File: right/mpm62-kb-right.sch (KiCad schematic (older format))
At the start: 72 parts, among them J1 Conn_01x04_Male, SW1 SW_Push, U1 MCP23018-E_SP

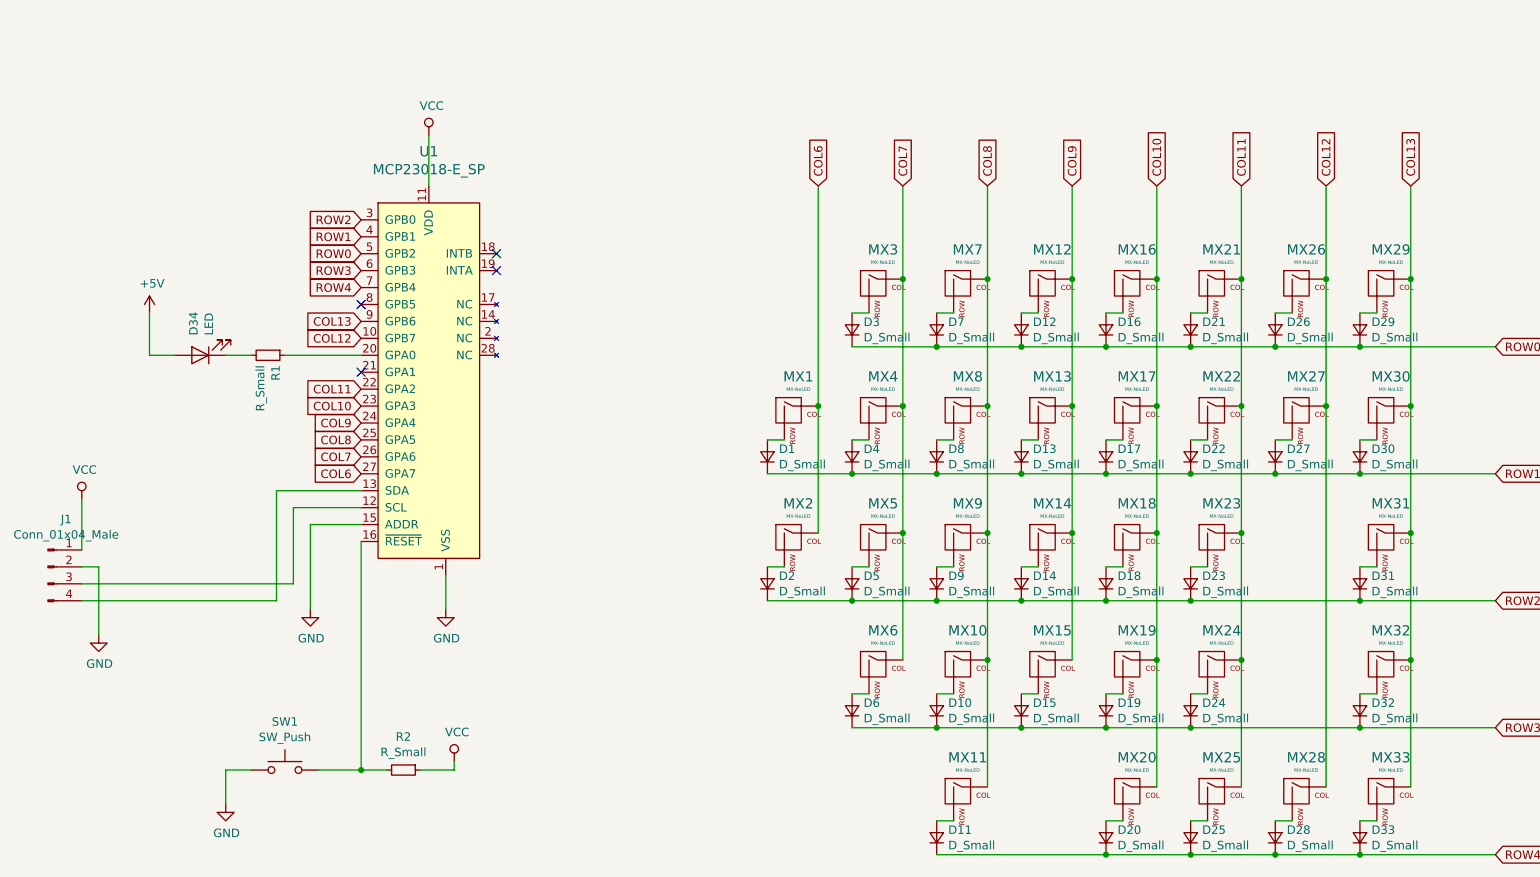
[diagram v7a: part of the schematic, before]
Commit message: Fix issues on right side: 1. Remove reset switch and connect reset directly to vcc - switch was not useful and added complexity. 2. Inverted spacebar stabilizer holes (previous commit did not mention that this was done also on the left side). 3. LED was connected to wrong power bus. 4. Resistor size was smaller than typical TH resistors. 5. Add header pins for ground and vcc for debugging. 6. Some minor routing cleanups.
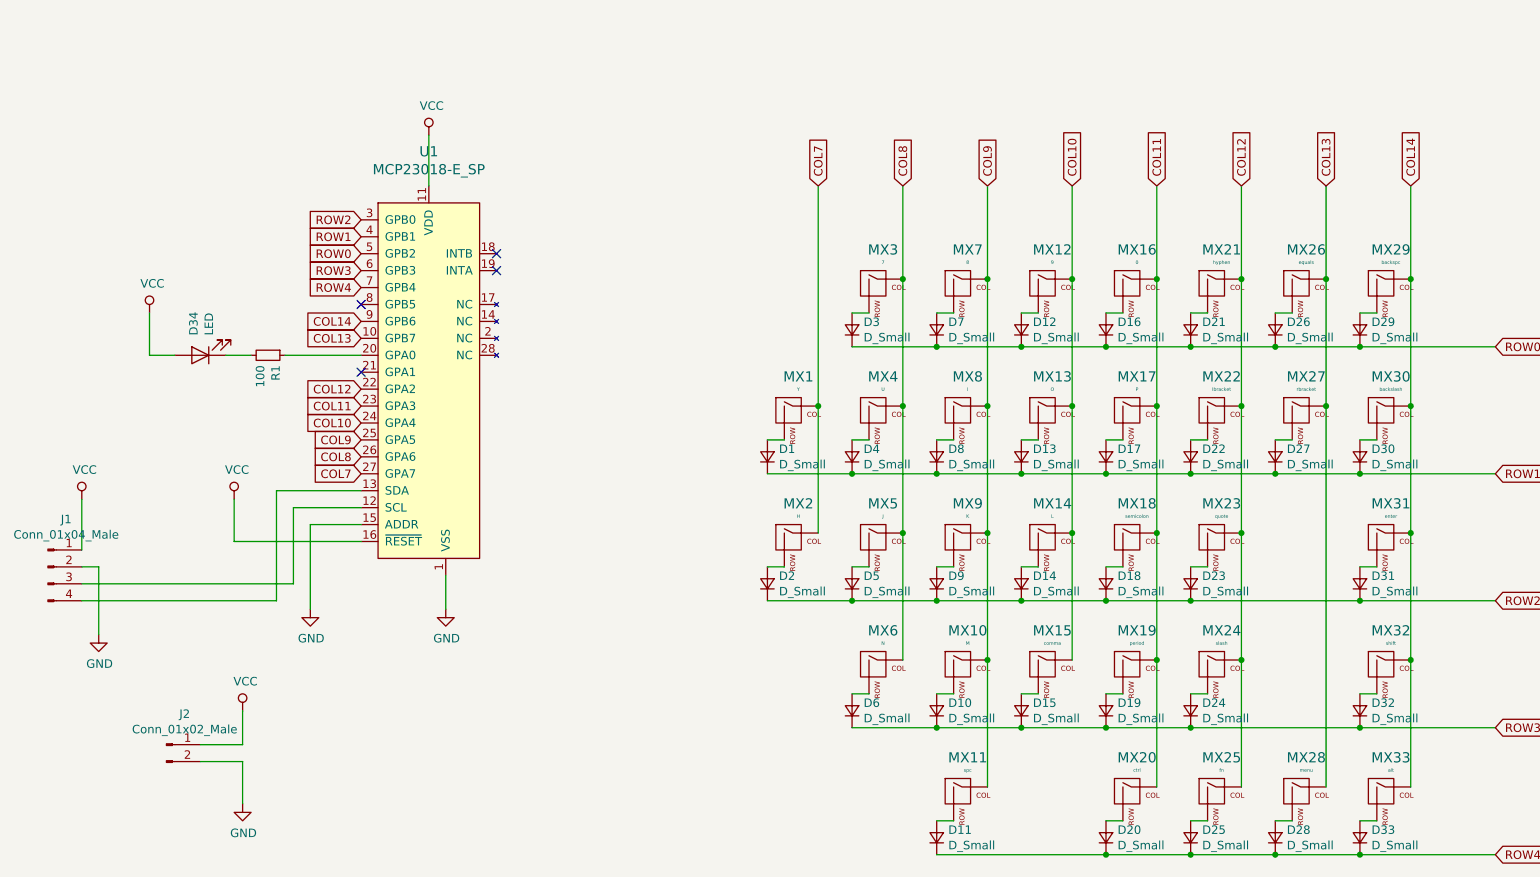
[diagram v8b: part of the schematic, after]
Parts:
- removed R2: R_Small, Resistor_THT:R_Axial_DIN0204_L3.6mm_D1.6mm_P5.08mm_Horizontal, symbol Device:R_Small
- removed SW1: SW_Push, random-keyboard-parts:SKQG-1155865, symbol Switch:SW_Push
- added J2: Conn_01x02_Male, Connector_PinHeader_2.54mm:PinHeader_1x02_P2.54mm_Vertical, symbol Connector:Conn_01x02_Male
- MX1: value MX-NoLED -> Y
- MX10: value MX-NoLED -> M
- MX11: value MX-NoLED -> spc; footprint MX_Alps_Hybrid:MX-3U-NoLED -> MX_Alps_Hybrid:MX-3U-ReversedStabilizers-NoLED
- MX12: value MX-NoLED -> 9
- MX13: value MX-NoLED -> O
- MX14: value MX-NoLED -> L
- MX15: value MX-NoLED -> comma
- MX16: value MX-NoLED -> 0
- MX17: value MX-NoLED -> P
- MX18: value MX-NoLED -> semicolon
- MX19: value MX-NoLED -> period
- MX2: value MX-NoLED -> H
- MX20: value MX-NoLED -> ctrl
- MX21: value MX-NoLED -> hyphen
- MX22: value MX-NoLED -> lbracket
- MX23: value MX-NoLED -> quote
- MX24: value MX-NoLED -> slash
- MX25: value MX-NoLED -> fn
- MX26: value MX-NoLED -> equals
- MX27: value MX-NoLED -> rbracket
- MX28: value MX-NoLED -> menu
- MX29: value MX-NoLED -> backspc
- MX3: value MX-NoLED -> 7
- MX30: value MX-NoLED -> backslash
- MX31: value MX-NoLED -> enter
- MX32: value MX-NoLED -> shift
- MX33: value MX-NoLED -> alt
- MX4: value MX-NoLED -> U
- MX5: value MX-NoLED -> J
- MX6: value MX-NoLED -> N
- MX7: value MX-NoLED -> 8
- MX8: value MX-NoLED -> I
- MX9: value MX-NoLED -> K
- R1: value R_Small -> 100; footprint Resistor_THT:R_Axial_DIN0204_L3.6mm_D1.6mm_P5.08mm_Horizontal -> Resistor_THT:R_Axial_DIN0207_L6.3mm_D2.5mm_P7.62mm_Horizontal
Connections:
- net +5V is gone; now on net VCC: D34.2 (A)
- net COL6 is gone; now on net COL7: MX1.1 (COL), MX2.1 (COL), U1.27 (GPA7)
- net COL10: now also MX12.1 (COL), MX13.1 (COL), MX14.1 (COL), MX15.1 (COL), U1.24 (GPA4); no longer MX16.1 (COL), MX17.1 (COL), MX18.1 (COL), MX19.1 (COL), MX20.1 (COL), U1.23 (GPA3)
- net COL11: now also MX16.1 (COL), MX17.1 (COL), MX18.1 (COL), MX19.1 (COL), MX20.1 (COL), U1.23 (GPA3); no longer MX21.1 (COL), MX22.1 (COL), MX23.1 (COL), MX24.1 (COL), MX25.1 (COL), U1.22 (GPA2)
- net COL12: now also MX21.1 (COL), MX22.1 (COL), MX23.1 (COL), MX24.1 (COL), MX25.1 (COL), U1.22 (GPA2); no longer MX26.1 (COL), MX27.1 (COL), MX28.1 (COL), U1.10 (GPB7)
- net COL13: now also MX26.1 (COL), MX27.1 (COL), MX28.1 (COL), U1.10 (GPB7); no longer MX29.1 (COL), MX30.1 (COL), MX31.1 (COL), MX32.1 (COL), MX33.1 (COL), U1.9 (GPB6)
- net COL7: no longer MX3.1 (COL), MX4.1 (COL), MX5.1 (COL), MX6.1 (COL), U1.26 (GPA6)
- net COL8: now also MX3.1 (COL), MX4.1 (COL), MX5.1 (COL), MX6.1 (COL), U1.26 (GPA6); no longer MX10.1 (COL), MX11.1 (COL), MX7.1 (COL), MX8.1 (COL), MX9.1 (COL), U1.25 (GPA5)
- net COL9: now also MX10.1 (COL), MX11.1 (COL), MX7.1 (COL), MX8.1 (COL), MX9.1 (COL), U1.25 (GPA5); no longer MX12.1 (COL), MX13.1 (COL), MX14.1 (COL), MX15.1 (COL), U1.24 (GPA4)
- net GND: now also J2.2 (Pin_2)
- net VCC: now also U1.16 (~RESET), J2.1 (Pin_1)
- new net COL14: MX29.1 (COL), MX30.1 (COL), MX31.1 (COL), MX32.1 (COL), MX33.1 (COL), U1.9 (GPB6)
